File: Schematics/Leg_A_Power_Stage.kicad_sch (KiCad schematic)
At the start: 38 parts, among them Q2 C3M0025065K, Q3 C3M0025065K, U1 UCC21710QDWRQ1, U2 UCC21710QDWRQ1

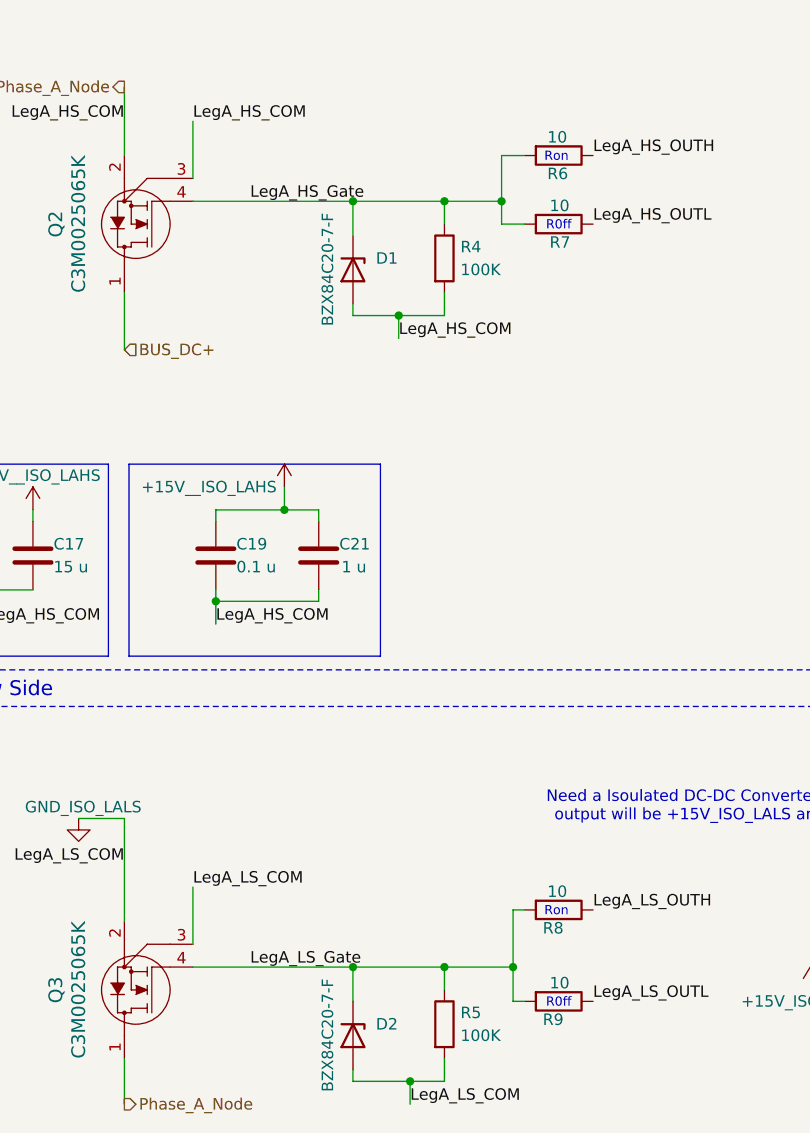
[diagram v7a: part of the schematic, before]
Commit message: [Milestone Compelted Controller and USB]
- Added Test Points
- Completed USB circuit to Controller
- Wired up Controller
- Added Connectors to Power Subsheet and 12pin from cotnroller to Full
  Bridge
- Added 3d models for USB compoents
- General fixes to subsheets
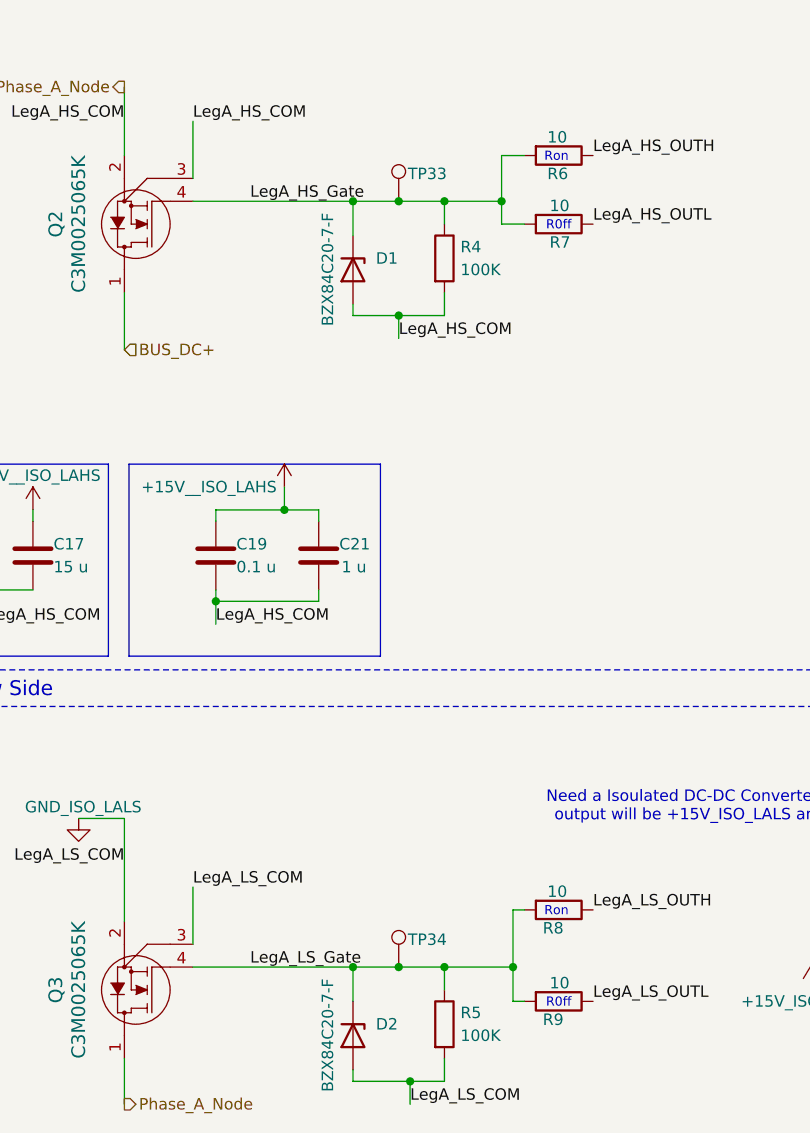
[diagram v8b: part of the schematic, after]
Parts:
- added TP33, TP34: 5277, SiC_Inverter:5277, symbol SiC_Inverter:5277
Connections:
- net LegA_HS_Gate: now also TP33.1
- net LegA_LS_Gate: now also TP34.1
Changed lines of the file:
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@@
 	)
 	(junction
+		(at 66.04 140.97)
+		(diameter 0)
+		(color 0 0 0 0)
+	)
+	(junction
+		(at 66.04 55.88)
+		(diameter 0)
+		(color 0 0 0 0)
+	)
+	(junction
 		(at 182.88 71.12)
 		(diameter 0)
@@
 	(wire
 		(pts
-			(xy 60.96 55.88) (xy 71.12 55.88)
+			(xy 60.96 55.88) (xy 66.04 55.88)
 		)
 		(stroke
@@
 	(wire
 		(pts
+			(xy 66.04 55.88) (xy 71.12 55.88)
+		)
+		(stroke
+			(width 0)
+			(type default)
+		)
+	)
+	(wire
+		(pts
 			(xy 20.32 99.06) (xy 20.32 102.87)
 		)
@@
 	(wire
 		(pts
-			(xy 60.96 140.97) (xy 71.12 140.97)
+			(xy 60.96 140.97) (xy 66.04 140.97)
 		)
 		(stroke
@@
 	(wire
 		(pts
+			(xy 66.04 140.97) (xy 71.12 140.97)
+		)
+		(stroke
+			(width 0)
+			(type default)
+		)
+	)
+	(wire
+		(pts
 			(xy 146.05 64.77) (xy 148.59 64.77)
 		)
@@
 	)
 	(symbol
+		(lib_id "SiC_Inverter:5277")
+		(at 66.04 55.88 0)
+		(unit 1)
+		(exclude_from_sim no)
+		(in_bom yes)
+		(on_board yes)
+		(dnp no)
+		(property "Reference" "TP33"
+			(at 67.056 52.832 0)
+			(effects
+				(font
+					(size 1.27 1.27)
+				)
+				(justify left)
+			)
+		)
+		(property "Value" "5277"
+			(at 50.038 68.834 0)
+			(effects
+				(font
+					(size 1.27 1.27)
+				)
+				(hide yes)
+			)
+		)
+		(property "Footprint" "SiC_Inverter:5277"
+			(at 56.134 67.056 0)
+			(effects
+				(font
+					(size 1.27 1.27)
+				)
+				(hide yes)
+			)
+		)
+		(property "Datasheet" "https://www.keyelco.com/userAssets/file/K75p62.pdf"
+			(at 73.914 63.246 0)
+			(effects
+				(font
+					(size 1.27 1.27)
+				)
+				(hide yes)
+			)
+		)
+		(property "Description" "Test Plugs & Test Jacks TEST POINT (BLUE) - COMPACT"
+			(at 76.454 65.278 0)
+			(effects
+				(font
+					(size 1.27 1.27)
+				)
+				(hide yes)
+			)
+		)
+		(pin "1"
+		)
+		(instances
+			(project "SiC_Single_Phase_Inverter"
+				(path "/a1ed0539-9735-4ad1-a8fd-87e26e7fce16/b6e78e1f-718a-4f31-892b-d9c389541b0d/df0e594b-c560-4977-9819-59c4a1d47101"
+					(reference "TP33")
+					(unit 1)
+				)
+			)
+		)
+	)
+	(symbol
 		(lib_id "SiC_Inverter:RT1206BRD075KL")
 		(at 175.26 129.54 0)
@@
 					(unit 1)
 				)
+			)
+		)
+	)
+	(symbol
+		(lib_id "SiC_Inverter:5277")
+		(at 66.04 140.97 0)
+		(unit 1)
+		(exclude_from_sim no)
+		(in_bom yes)
+		(on_board yes)
+		(dnp no)
+		(property "Reference" "TP34"
+			(at 67.056 137.922 0)
+			(effects
+				(font
+					(size 1.27 1.27)
+				)
+				(justify left)
+			)
+		)
+		(property "Value" "5277"
+			(at 50.038 153.924 0)
+			(effects
+				(font
+					(size 1.27 1.27)
+				)
+				(hide yes)
+			)
+		)
+		(property "Footprint" "SiC_Inverter:5277"
+			(at 56.134 152.146 0)
+			(effects
+				(font
+					(size 1.27 1.27)
+				)
+				(hide yes)
+			)
+		)
+		(property "Datasheet" "https://www.keyelco.com/userAssets/file/K75p62.pdf"
+			(at 73.914 148.336 0)
+			(effects
+				(font
+					(size 1.27 1.27)
+				)
+				(hide yes)
+			)
+		)
+		(property "Description" "Test Plugs & Test Jacks TEST POINT (BLUE) - COMPACT"
+			(at 76.454 150.368 0)
+			(effects
+				(font
+					(size 1.27 1.27)
+				)
+				(hide yes)
+			)
+		)
+		(pin "1"
+		)
+		(instances
+			(project "SiC_Single_Phase_Inverter"
+				(path "/a1ed0539-9735-4ad1-a8fd-87e26e7fce16/b6e78e1f-718a-4f31-892b-d9c389541b0d/df0e594b-c560-4977-9819-59c4a1d47101"
+					(reference "TP34")
+					(unit 1)
+				)
